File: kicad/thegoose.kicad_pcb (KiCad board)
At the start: 4 copper layers, 88.5 x 47 mm, 175 parts, among them J1 USB_C_Receptacle_USB2.0_16P, J11 Balance, J12 LED stick, J3 XT30U-M pigtail 16AWG, J4 USB-A host, J5 IO 3x6 RA, Q1 AO4407A, Q2 80N03F, Q3 80N03F, SW1 Power, SW2 BOOT, U1 DRV8848, U10 RP2354A, U11 SRV05-4, U12 SY6280AAC, U13 BQ7791501, U14 74AHCT1G125, U2 DRV8848, U3 DRV8848, U4 AP64500SP-13, U5 CH224A, U6 SRV05-4, U7 BQ25798, U8 HT7550-1, U9 XC6206P332MR, Y1 12MHz

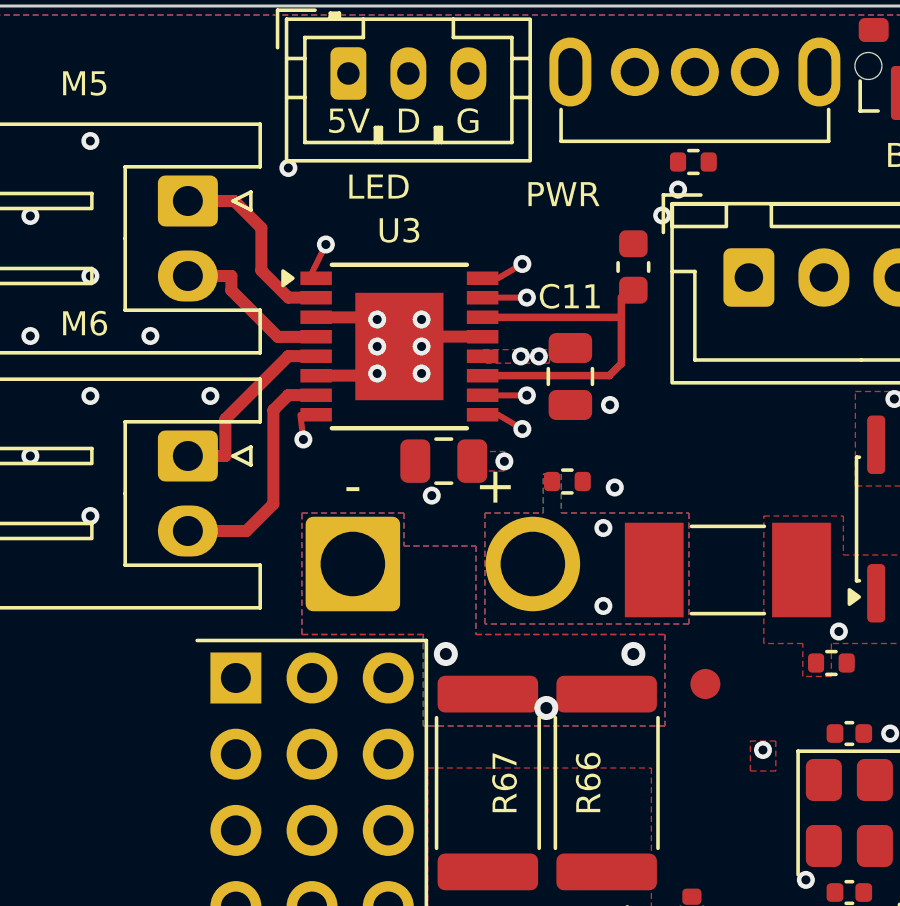
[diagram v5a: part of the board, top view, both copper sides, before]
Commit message: Use a vertical XT30 on the board instead of the pack pigtail
J3 is now an Amass XT30UPB-M (male, vertical, C428721) that the pack's
female XT30U-F plugs straight into; the pigtail pads and the reserved
mated-pair strip are removed and the pack power path re-routed.

The mated connector plus the 16 AWG bend needs 22.1-24.1 mm above the
board against 23.4 mm under the face of the 30 mm box. That is logged as
an enclosure open item to settle on the first prototype.

Schematic review passes; PCB review passes every gate except unrouted.

Co-Authored-By: Claude Opus 5.5 <noreply@anthropic.com>
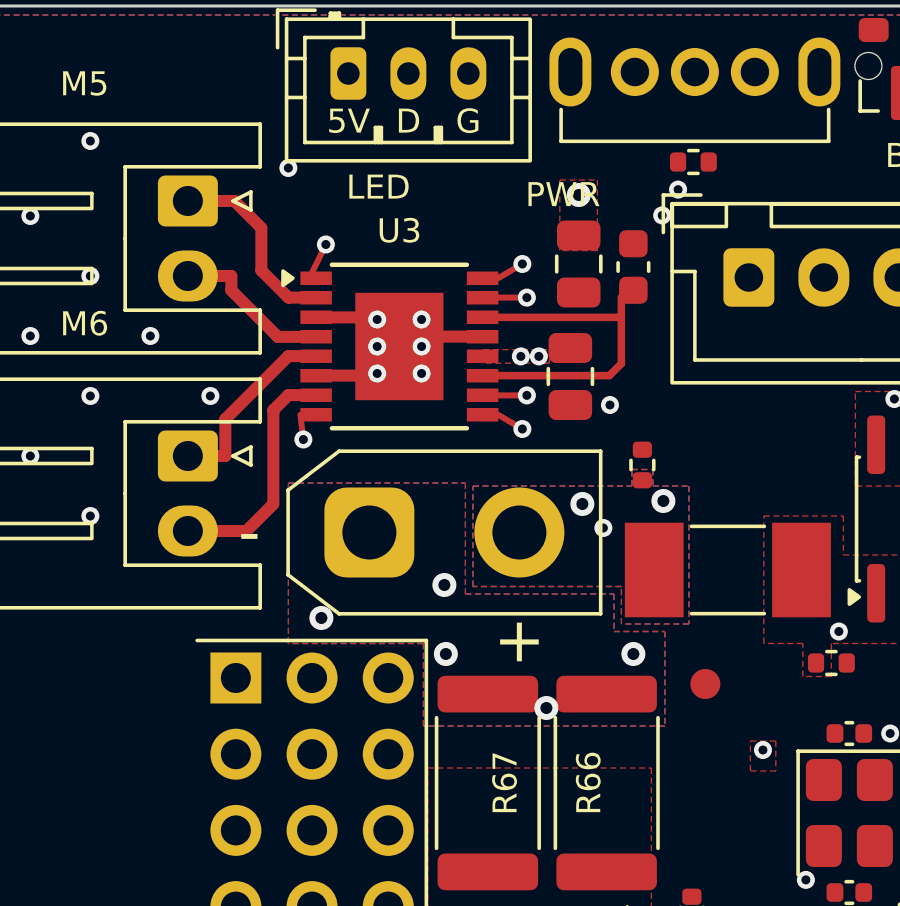
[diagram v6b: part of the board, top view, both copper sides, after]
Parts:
- J3: value XT30U-M pigtail 16AWG -> XT30UPB-M; footprint Connector_Wire:SolderWire-1.5sqmm_1x02_P6mm_D1.7mm_OD3mm -> hexy:AMASS_XT30UPB-M_1x02_P5.0mm_Vertical_EasyEDA3D
- moved C10 7.96 mm to (119.8, 108.6), turned to 90 degrees
- moved R61 2.56 mm to (121.9, 115.3), turned to 90 degrees
- moved J3 1.19 mm to (112.8, 117.5)
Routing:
- net GND: vias 172 -> 170
- net /Power & charging/PACK+: vias 2 -> 3
- net /Power & charging/BAT_N: vias 3 -> 5
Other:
- board text added: "J3 XT30UPB-M (male, vertical): the pack's XT30U-F plugs in from above; mated + 16 AWG bend 22.1-24.1 mm vs 23.4 under the face (enclosure open item)"
- board text removed: "XT30 MATED PAIR (about 20 x 10.2 x 5.2 plus leads): on edge over the shunts/FETs, beside the pack's lead end"
- board text removed: "XT30U-M PIGTAIL"
